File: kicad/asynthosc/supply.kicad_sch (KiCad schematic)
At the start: 48 parts, among them J1 USB_B_Micro, J2 Conn_02x05_Odd_Even, U1 LM1117S-3.3, U2 LMR62421XMF, U3 USBLC6-2SC6, U4 LM1117S-5.0, U5 Si1869DH

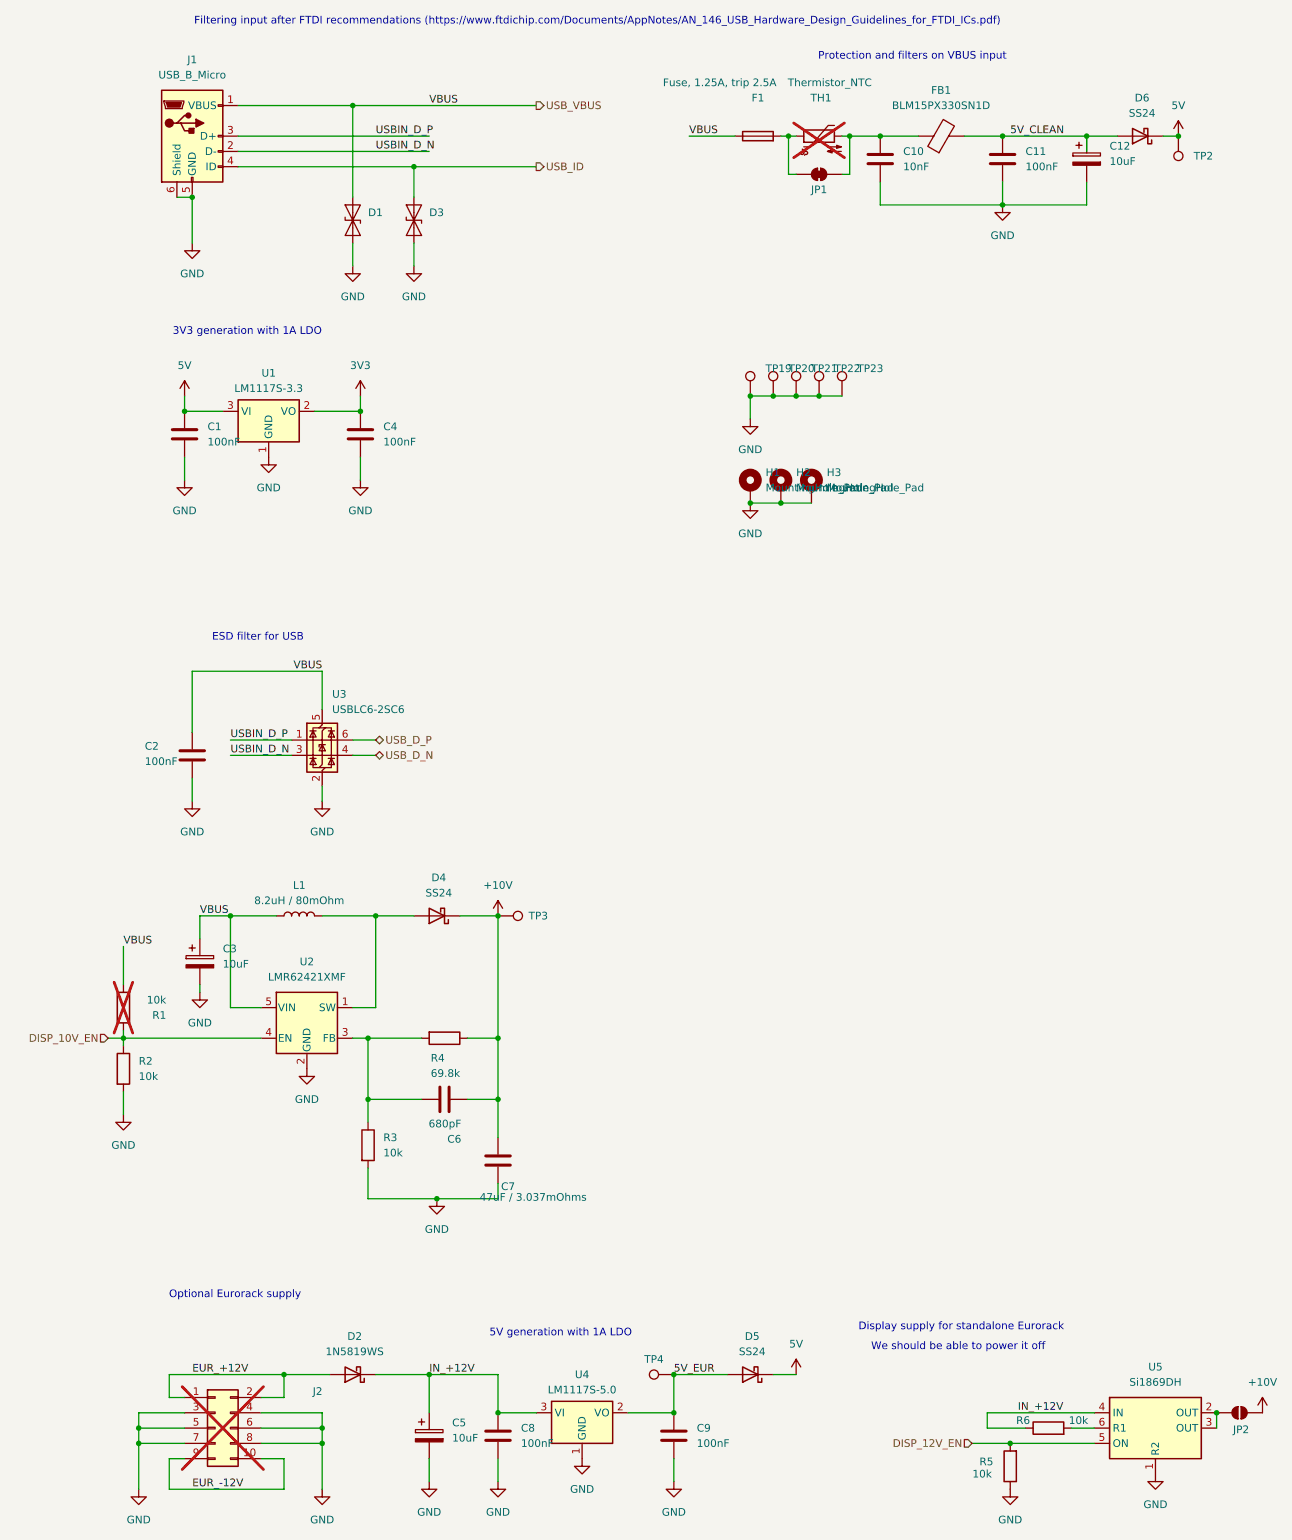
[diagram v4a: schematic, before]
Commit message: pcb: place and change some components for easier routing
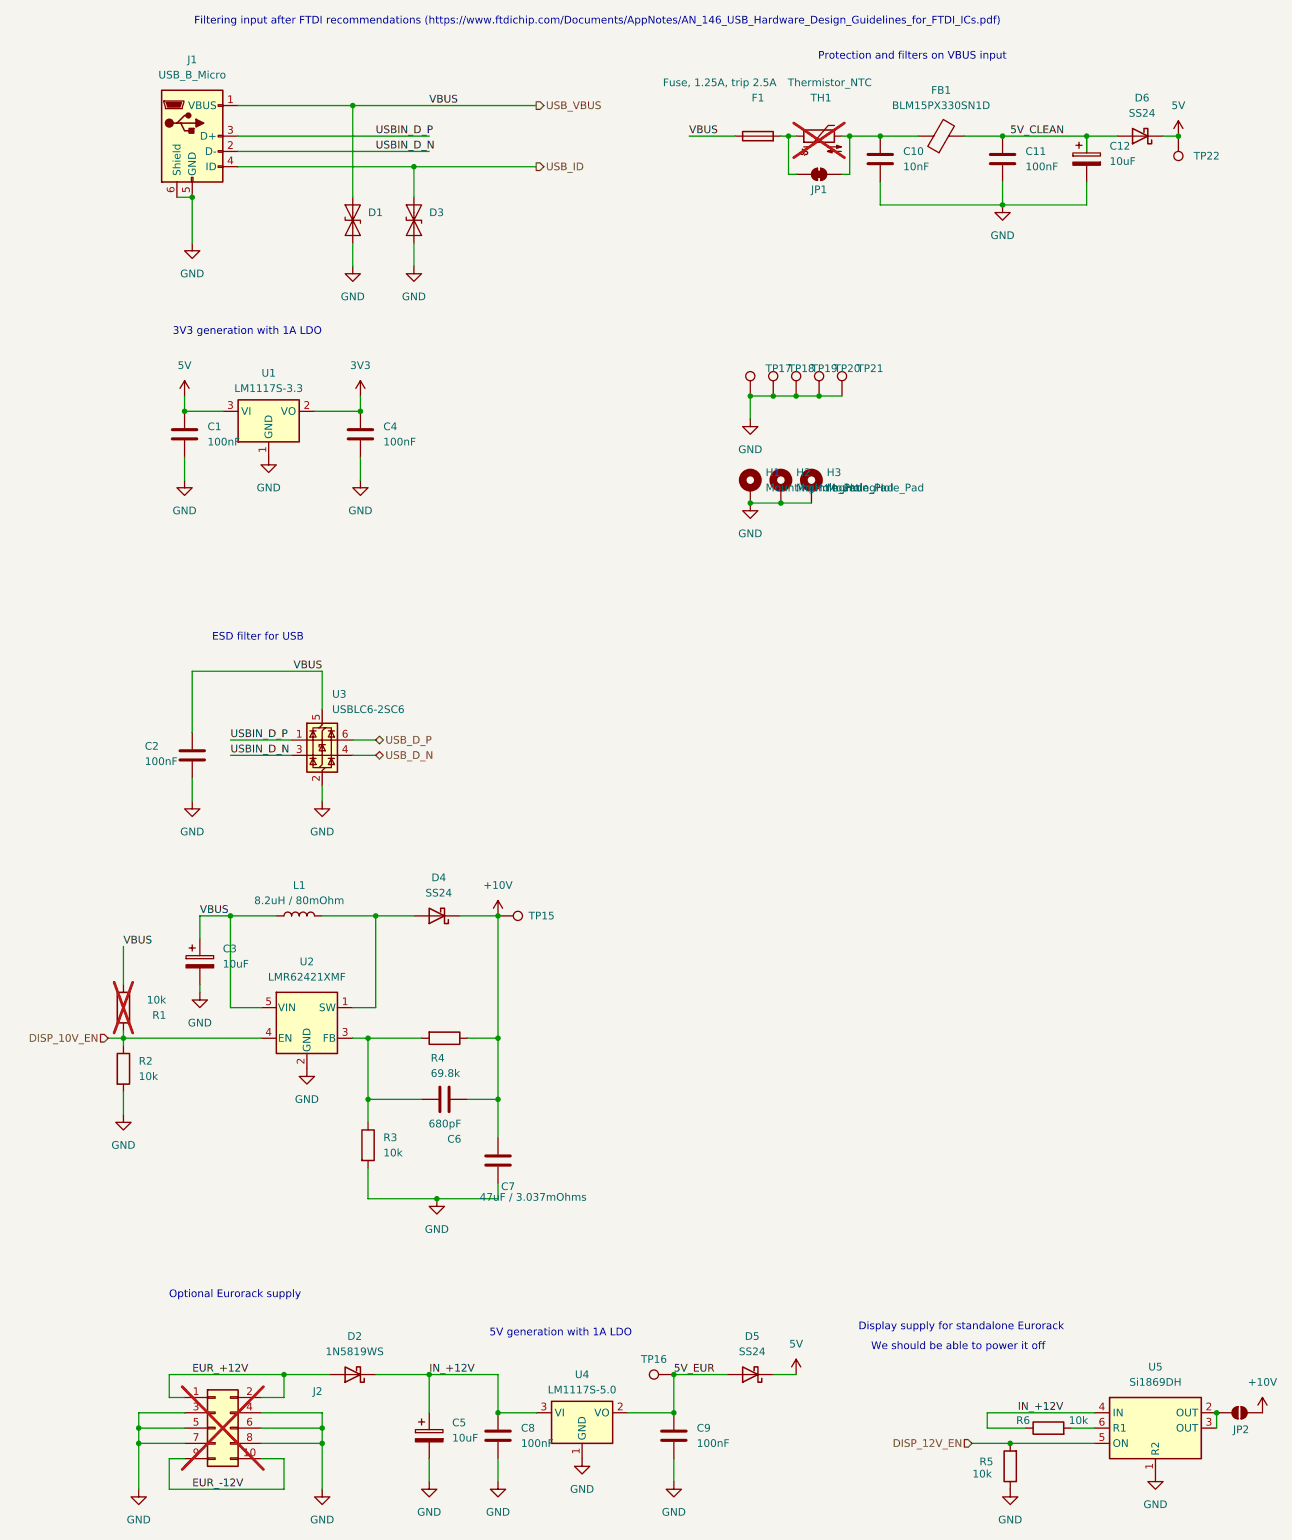
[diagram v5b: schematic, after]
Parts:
- renumbered TP3 to TP15, TP4 to TP16, TP19 to TP17, TP20 to TP18, TP21 to TP19, TP22 to TP20, TP23 to TP21, TP2 to TP22
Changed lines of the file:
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@@
 		(dnp no)
 		(fields_autoplaced yes)
-		(property "Reference" "TP23"
+		(property "Reference" "TP21"
 			(at 151.13 81.7879 0)
 			(effects
@@
 			(project "asynthosc"
 				(path "/d73e377a-a016-415f-8824-91cc6e4907b9/22ca5166-338c-4a24-8f8a-545e4a0286bf"
-					(reference "TP23")
+					(reference "TP21")
 					(unit 1)
 				)
@@
 		(dnp no)
 		(fields_autoplaced yes)
-		(property "Reference" "#PWR022"
+		(property "Reference" "#PWR024"
 			(at 140.97 252.73 0)
 			(effects
@@
 			(project "asynthosc"
 				(path "/d73e377a-a016-415f-8824-91cc6e4907b9/22ca5166-338c-4a24-8f8a-545e4a0286bf"
-					(reference "#PWR022")
+					(reference "#PWR024")
 					(unit 1)
 				)
@@
 		(dnp no)
 		(fields_autoplaced yes)
-		(property "Reference" "TP2"
+		(property "Reference" "TP22"
 			(at 207.01 46.4819 0)
 			(effects
@@
 			(project "asynthosc"
 				(path "/d73e377a-a016-415f-8824-91cc6e4907b9/22ca5166-338c-4a24-8f8a-545e4a0286bf"
-					(reference "TP2")
+					(reference "TP22")
 					(unit 1)
 				)
@@
 		(dnp no)
 		(fields_autoplaced yes)
-		(property "Reference" "#PWR026"
+		(property "Reference" "#PWR028"
 			(at 204.47 46.99 0)
 			(effects
@@
 			(project "asynthosc"
 				(path "/d73e377a-a016-415f-8824-91cc6e4907b9/22ca5166-338c-4a24-8f8a-545e4a0286bf"
-					(reference "#PWR026")
+					(reference "#PWR028")
 					(unit 1)
 				)
@@
 		(dnp no)
 		(fields_autoplaced yes)
-		(property "Reference" "TP20"
+		(property "Reference" "TP18"
 			(at 139.7 81.7879 0)
 			(effects
@@
 			(project "asynthosc"
 				(path "/d73e377a-a016-415f-8824-91cc6e4907b9/22ca5166-338c-4a24-8f8a-545e4a0286bf"
-					(reference "TP20")
+					(reference "TP18")
 					(unit 1)
 				)
@@
 		(dnp no)
 		(fields_autoplaced yes)
-		(property "Reference" "TP22"
+		(property "Reference" "TP20"
 			(at 147.32 81.7879 0)
 			(effects
@@
 			(project "asynthosc"
 				(path "/d73e377a-a016-415f-8824-91cc6e4907b9/22ca5166-338c-4a24-8f8a-545e4a0286bf"
-					(reference "TP22")
+					(reference "TP20")
 					(unit 1)
 				)
@@
 		(dnp no)
 		(fields_autoplaced yes)
-		(property "Reference" "#PWR027"
+		(property "Reference" "#PWR029"
 			(at 218.44 259.08 0)
 			(effects
@@
 			(project "asynthosc"
 				(path "/d73e377a-a016-415f-8824-91cc6e4907b9/22ca5166-338c-4a24-8f8a-545e4a0286bf"
-					(reference "#PWR027")
+					(reference "#PWR029")
 					(unit 1)
 				)
@@
 		(dnp no)
 		(fields_autoplaced yes)
-		(property "Reference" "TP4"
+		(property "Reference" "TP16"
 			(at 117.348 246.38 90)
 			(effects
@@
 			(project "asynthosc"
 				(path "/d73e377a-a016-415f-8824-91cc6e4907b9/22ca5166-338c-4a24-8f8a-545e4a0286bf"
-					(reference "TP4")
+					(reference "TP16")
 					(unit 1)
 				)
@@
 		(dnp no)
 		(fields_autoplaced yes)
-		(property "Reference" "#PWR025"
+		(property "Reference" "#PWR027"
 			(at 200.66 271.78 0)
 			(effects
@@
 			(project "asynthosc"
 				(path "/d73e377a-a016-415f-8824-91cc6e4907b9/22ca5166-338c-4a24-8f8a-545e4a0286bf"
-					(reference "#PWR025")
+					(reference "#PWR027")
 					(unit 1)
 				)
@@
 		(dnp no)
 		(fields_autoplaced yes)
-		(property "Reference" "TP3"
+		(property "Reference" "TP15"
 			(at 96.52 172.7199 90)
 			(effects
@@
 			(project "asynthosc"
 				(path "/d73e377a-a016-415f-8824-91cc6e4907b9/22ca5166-338c-4a24-8f8a-545e4a0286bf"
-					(reference "TP3")
+					(reference "TP15")
 					(unit 1)
 				)
@@
 		(dnp no)
 		(fields_autoplaced yes)
-		(property "Reference" "#PWR024"
+		(property "Reference" "#PWR026"
 			(at 176.53 274.32 0)
 			(effects
@@
 			(project "asynthosc"
 				(path "/d73e377a-a016-415f-8824-91cc6e4907b9/22ca5166-338c-4a24-8f8a-545e4a0286bf"
-					(reference "#PWR024")
+					(reference "#PWR026")
 					(unit 1)
 				)
@@
 		(dnp no)
 		(fields_autoplaced yes)
-		(property "Reference" "TP19"
+		(property "Reference" "TP17"
 			(at 135.89 81.7879 0)
 			(effects
@@
 			(project "asynthosc"
 				(path "/d73e377a-a016-415f-8824-91cc6e4907b9/22ca5166-338c-4a24-8f8a-545e4a0286bf"
-					(reference "TP19")
+					(reference "TP17")
 					(unit 1)
 				)
@@
 		(dnp no)
 		(fields_autoplaced yes)
-		(property "Reference" "TP21"
+		(property "Reference" "TP19"
 			(at 143.51 81.7879 0)
 			(effects
@@
 			(project "asynthosc"
 				(path "/d73e377a-a016-415f-8824-91cc6e4907b9/22ca5166-338c-4a24-8f8a-545e4a0286bf"
-					(reference "TP21")
+					(reference "TP19")
 					(unit 1)
 				)
@@
 		(dnp no)
 		(fields_autoplaced yes)
-		(property "Reference" "#PWR023"
+		(property "Reference" "#PWR025"
 			(at 175.26 60.96 0)
 			(effects
@@
 			(project "asynthosc"
 				(path "/d73e377a-a016-415f-8824-91cc6e4907b9/22ca5166-338c-4a24-8f8a-545e4a0286bf"
-					(reference "#PWR023")
+					(reference "#PWR025")
 					(unit 1)
 				)
@@
 		(dnp no)
 		(fields_autoplaced yes)
-		(property "Reference" "#PWR0146"
+		(property "Reference" "#PWR023"
 			(at 133.35 110.49 0)
 			(effects
@@
 			(project "asynthosc"
 				(path "/d73e377a-a016-415f-8824-91cc6e4907b9/22ca5166-338c-4a24-8f8a-545e4a0286bf"
-					(reference "#PWR0146")
+					(reference "#PWR023")
 					(unit 1)
 				)
@@
 		(dnp no)
 		(fields_autoplaced yes)
-		(property "Reference" "#PWR0145"
+		(property "Reference" "#PWR022"
 			(at 133.35 96.52 0)
 			(effects
@@
 			(project ""
 				(path "/d73e377a-a016-415f-8824-91cc6e4907b9/22ca5166-338c-4a24-8f8a-545e4a0286bf"
-					(reference "#PWR0145")
+					(reference "#PWR022")
 					(unit 1)
 				)

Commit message: sch: pcb: tiny fixes and changes
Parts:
- added TP29, TP30: TestPoint, TestPoint:TestPoint_Pad_D1.0mm, symbol Connector:TestPoint
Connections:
- net 3V3: now also TP29.1
- net IN_+12V: now also TP30.1
- net USB_VBUS renamed VBUS
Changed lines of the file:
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@@
 	)
 	(junction
+		(at 77.47 248.92)
+		(diameter 0)
+		(color 0 0 0 0)
+	)
+	(junction
 		(at 120.65 255.27)
 		(diameter 0)
@@
 	(wire
 		(pts
-			(xy 71.12 248.92) (xy 80.01 248.92)
+			(xy 71.12 248.92) (xy 77.47 248.92)
 		)
 		(stroke
@@
 	(wire
 		(pts
+			(xy 77.47 248.92) (xy 80.01 248.92)
+		)
+		(stroke
+			(width 0)
+			(type default)
+		)
+	)
+	(wire
+		(pts
 			(xy 29.21 193.04) (xy 52.07 193.04)
 		)
@@
 		)
 	)
-	(hierarchical_label "USB_VBUS"
+	(hierarchical_label "VBUS"
 		(shape output)
 		(at 97.79 38.1 0)
@@
 	)
 	(symbol
+		(lib_id "Connector:TestPoint")
+		(at 77.47 248.92 0)
+		(unit 1)
+		(exclude_from_sim yes)
+		(in_bom yes)
+		(on_board yes)
+		(dnp no)
+		(fields_autoplaced yes)
+		(property "Reference" "TP30"
+			(at 80.01 245.6179 0)
+			(effects
+				(font
+					(size 1.27 1.27)
+				)
+				(justify left)
+			)
+		)
+		(property "Value" "TestPoint"
+			(at 80.01 246.8879 0)
+			(effects
+				(font
+					(size 1.27 1.27)
+				)
+				(justify left)
+				(hide yes)
+			)
+		)
+		(property "Footprint" "TestPoint:TestPoint_Pad_D1.0mm"
+			(at 82.55 248.92 0)
+			(effects
+				(font
+					(size 1.27 1.27)
+				)
+				(hide yes)
+			)
+		)
+		(property "Datasheet" "~"
+			(at 82.55 248.92 0)
+			(effects
+				(font
+					(size 1.27 1.27)
+				)
+				(hide yes)
+			)
+		)
+		(property "Description" "test point"
+			(at 77.47 248.92 0)
+			(effects
+				(font
+					(size 1.27 1.27)
+				)
+				(hide yes)
+			)
+		)
+		(property "LCSC" ""
+			(at 77.47 248.92 0)
+			(effects
+				(font
+					(size 1.27 1.27)
+				)
+				(hide yes)
+			)
+		)
+		(property "Manufacturer" ""
+			(at 77.47 248.92 0)
+			(effects
+				(font
+					(size 1.27 1.27)
+				)
+				(hide yes)
+			)
+		)
+		(property "RefNum" "_na_"
+			(at 77.47 248.92 0)
+			(effects
+				(font
+					(size 1.27 1.27)
+				)
+				(hide yes)
+			)
+		)
+		(pin "1"
+		)
+		(instances
+			(project "asynthosc"
+				(path "/d73e377a-a016-415f-8824-91cc6e4907b9/22ca5166-338c-4a24-8f8a-545e4a0286bf"
+					(reference "TP30")
+					(unit 1)
+				)
+			)
+		)
+	)
+	(symbol
 		(lib_id "Jumper:SolderJumper_2_Bridged")
 		(at 144.78 49.53 0)
@@
 					(unit 1)
 				)
+			)
+		)
+	)
+	(symbol
+		(lib_id "Connector:TestPoint")
+		(at 68.58 88.9 270)
+		(unit 1)
+		(exclude_from_sim yes)
+		(in_bom yes)
+		(on_board yes)
+		(dnp no)
+		(fields_autoplaced yes)
+		(property "Reference" "TP29"
+			(at 73.66 88.8999 90)
+			(effects
+				(font
+					(size 1.27 1.27)
+				)
+				(justify left)
+			)
+		)
+		(property "Value" "TestPoint"
+			(at 70.6121 91.44 0)
+			(effects
+				(font
+					(size 1.27 1.27)
+				)
+				(justify left)
+				(hide yes)
+			)
+		)
+		(property "Footprint" "TestPoint:TestPoint_Pad_D1.0mm"
+			(at 68.58 93.98 0)
+			(effects
+				(font
+					(size 1.27 1.27)
+				)
+				(hide yes)
+			)
+		)
+		(property "Datasheet" "~"
+			(at 68.58 93.98 0)
+			(effects
+				(font
+					(size 1.27 1.27)
+				)
+				(hide yes)
+			)
+		)
+		(property "Description" "test point"
+			(at 68.58 88.9 0)
+			(effects
+				(font
+					(size 1.27 1.27)
+				)
+				(hide yes)
+			)
+		)
+		(property "LCSC" ""
+			(at 68.58 88.9 0)
+			(effects
+				(font
+					(size 1.27 1.27)
+				)
+				(hide yes)
+			)
+		)
+		(property "Manufacturer" ""
+			(at 68.58 88.9 0)
+			(effects
+				(font
+					(size 1.27 1.27)
+				)
+				(hide yes)
+			)
+		)
+		(property "RefNum" "_na_"
+			(at 68.58 88.9 0)
+			(effects
+				(font
+					(size 1.27 1.27)
+				)
+				(hide yes)
+			)
+		)
+		(pin "1"
+		)
+		(instances
+			(project "asynthosc"
+				(path "/d73e377a-a016-415f-8824-91cc6e4907b9/22ca5166-338c-4a24-8f8a-545e4a0286bf"
+					(reference "TP29")
+					(unit 1)
+				)
